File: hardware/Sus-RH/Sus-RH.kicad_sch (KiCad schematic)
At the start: 40 parts, among them J1 MX150_02x06_Vertical, J2 53307-2471, J4 Conn_01x06, J5 Conn_01x06, U1 TLV9002QDRQ1, U2 LDO40LPURY

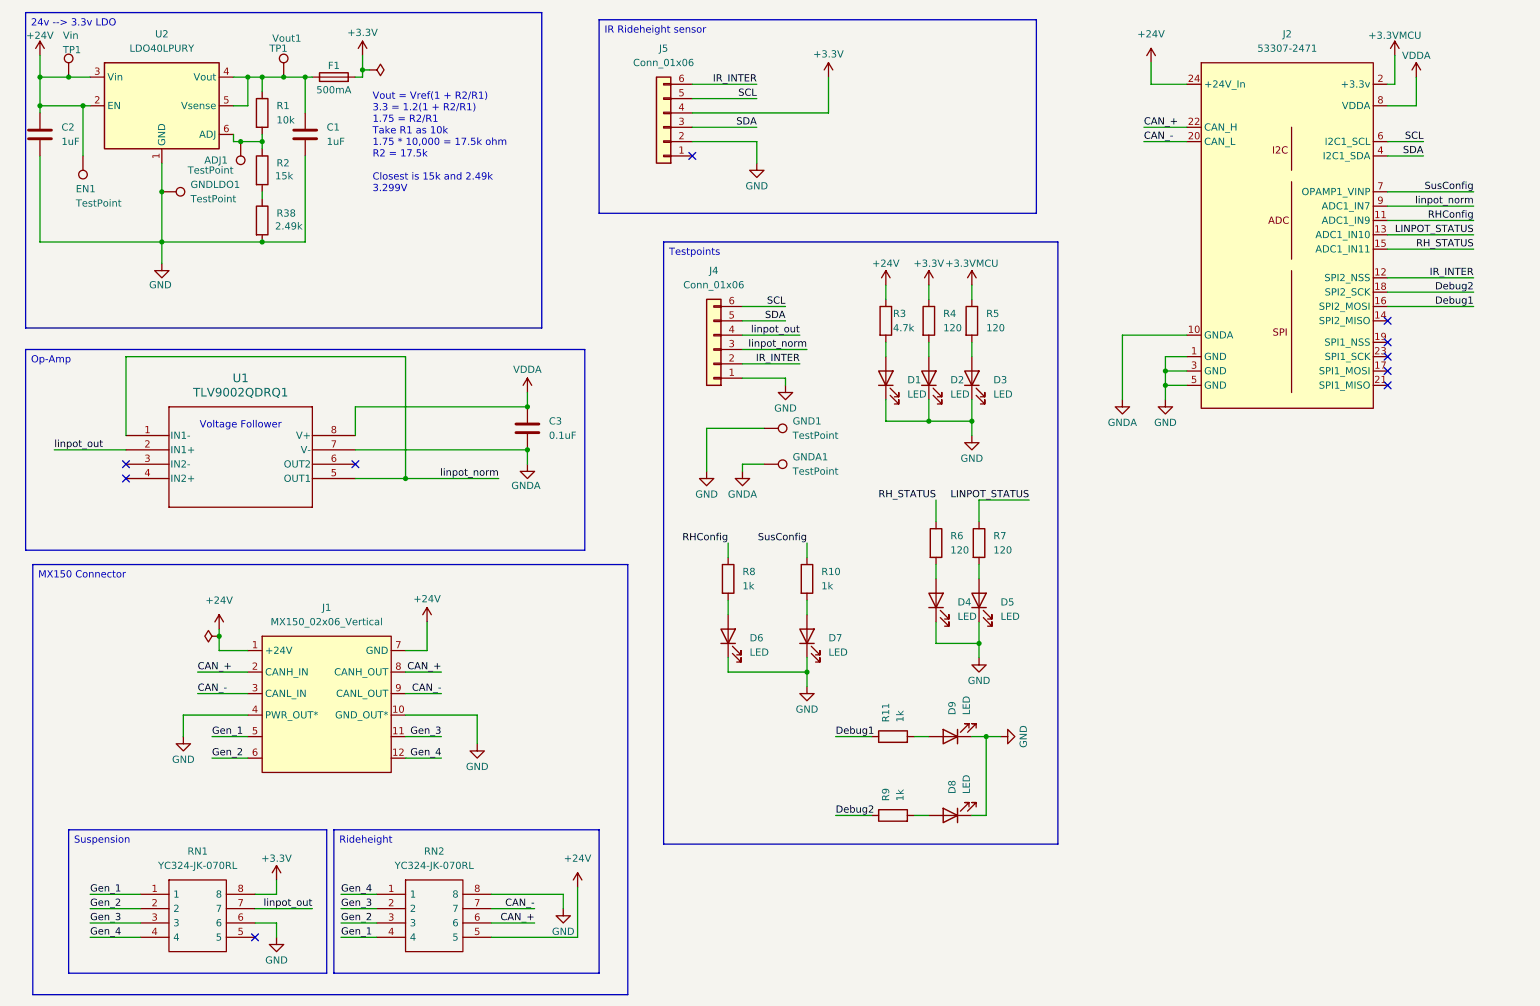
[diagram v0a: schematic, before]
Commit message: schematic changes: ldo switched out of qfn, op amp footprint fixed, resistor array changed. need add correct stm changes
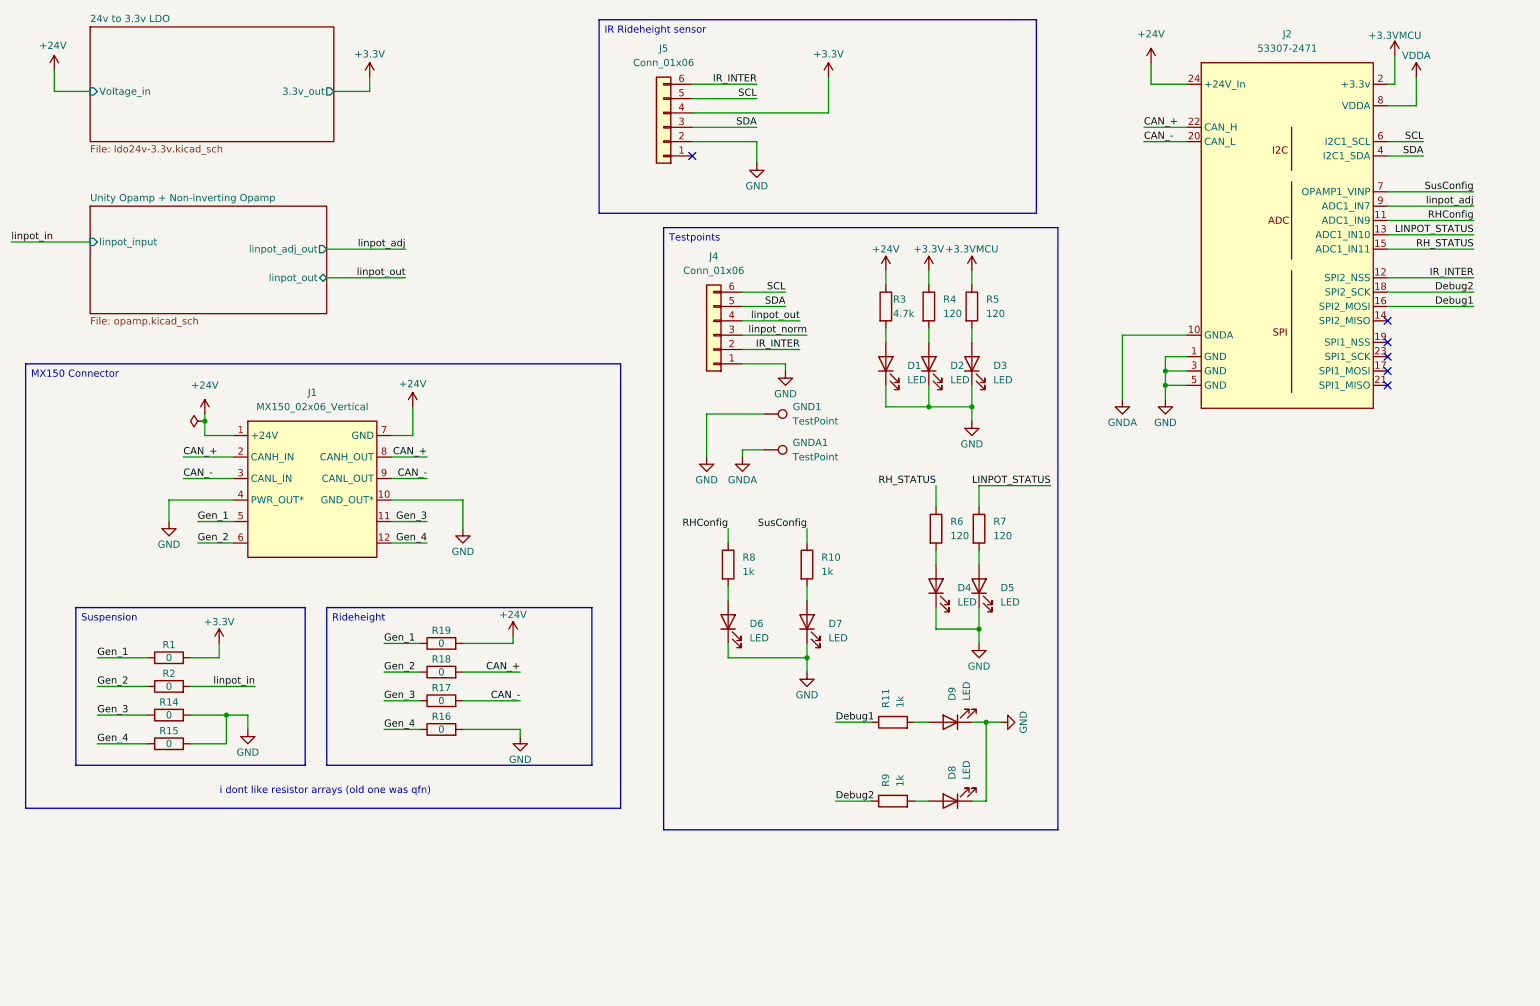
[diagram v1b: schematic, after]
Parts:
- removed ADJ1, EN1, GNDLDO1: TestPoint, TestPoint:TestPoint_Pad_D1.0mm, symbol Connector:TestPoint
- removed C1, C2: 1uF, Capacitor_SMD:C_0603_1608Metric_Pad1.08x0.95mm_HandSolder, symbol Device:C
- removed C3: 0.1uF, Capacitor_SMD:C_0603_1608Metric_Pad1.08x0.95mm_HandSolder, symbol Device:C
- removed F1: 500mA, Fuse:Fuseholder_Blade_Mini_Keystone_3568, symbol Device:Fuse
- removed R38: 2.49k, Resistor_SMD:R_0603_1608Metric_Pad0.98x0.95mm_HandSolder, symbol Device:R
- removed RN1, RN2: YC324-JK-070RL, 4pinRes:YC324JK07220RL, symbol YC324-JK-070RL:YC324-JK-070RL
- removed U1: TLV9002QDRQ1, footprints:SOIC8_D_TEX, symbol TLV9002QDRQ1:TLV9002QDRQ1
- removed U2: LDO40LPURY, Package_DFN_QFN:DFN-6-1EP_3x3mm_P0.95mm_EP1.7x2.6mm, symbol Regulator_Linear:LDO40LPURY
- removed Vin, Vout1: TP1, TestPoint:TestPoint_Pad_D1.0mm, symbol Connector:TestPoint
- added R14, R15, R16, R17, R18, R19: 0, symbol Device:R
- R1: value 10k -> 0; footprint Resistor_SMD:R_0603_1608Metric_Pad0.98x0.95mm_HandSolder -> (none); P/N CRCW060310K0FKEI -> (none)
- R2: value 15k -> 0; footprint Resistor_SMD:R_0603_1608Metric_Pad0.98x0.95mm_HandSolder -> (none); P/N CRCW060315K0FKEA -> (none)
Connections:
- net +24V: now also R19.2
- net +3.3V: now also R1.2
- net CAN_+: now also R18.2
- net CAN_-: now also R17.2
- net GND: now also R14.2, R15.2, R16.2
- net Gen_1: now also R1.1, R19.1
- net Gen_2: now also R2.1, R18.1
- net Gen_3: now also R14.1, R17.1
- net Gen_4: now also R15.1, R16.1
- net linpot_norm: no longer J2.9 (ADC1_IN7)
- net linpot_in: now reaches R2.2
- new net linpot_adj: J2.9 (ADC1_IN7)
- no-connect marks 10 -> 6
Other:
- added sheet 24v to 3.3v LDO (ldo24v-3.3v.kicad_sch)
- added sheet Unity Opamp + Non-inverting Opamp (opamp.kicad_sch)
- note added: "i dont like resistor arrays (old one was qfn)"
- note removed: "Voltage Follower"
- note removed: "Vout = Vref(1 + R2/R1) 3.3 = 1.2(1 + R2/R1) 1.75 = R2/R1 Take R1 as 10k 1.75 * 10,000 = 17.5k ohm R2 = 17.5k Closest is 15k and 2.49k 3.299V"
- moved on the sheet: D1, D2, D3, D4, D5, D6, D7, D8, D9, GND1, GNDA1, J1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

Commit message: finished sch + removed LDO
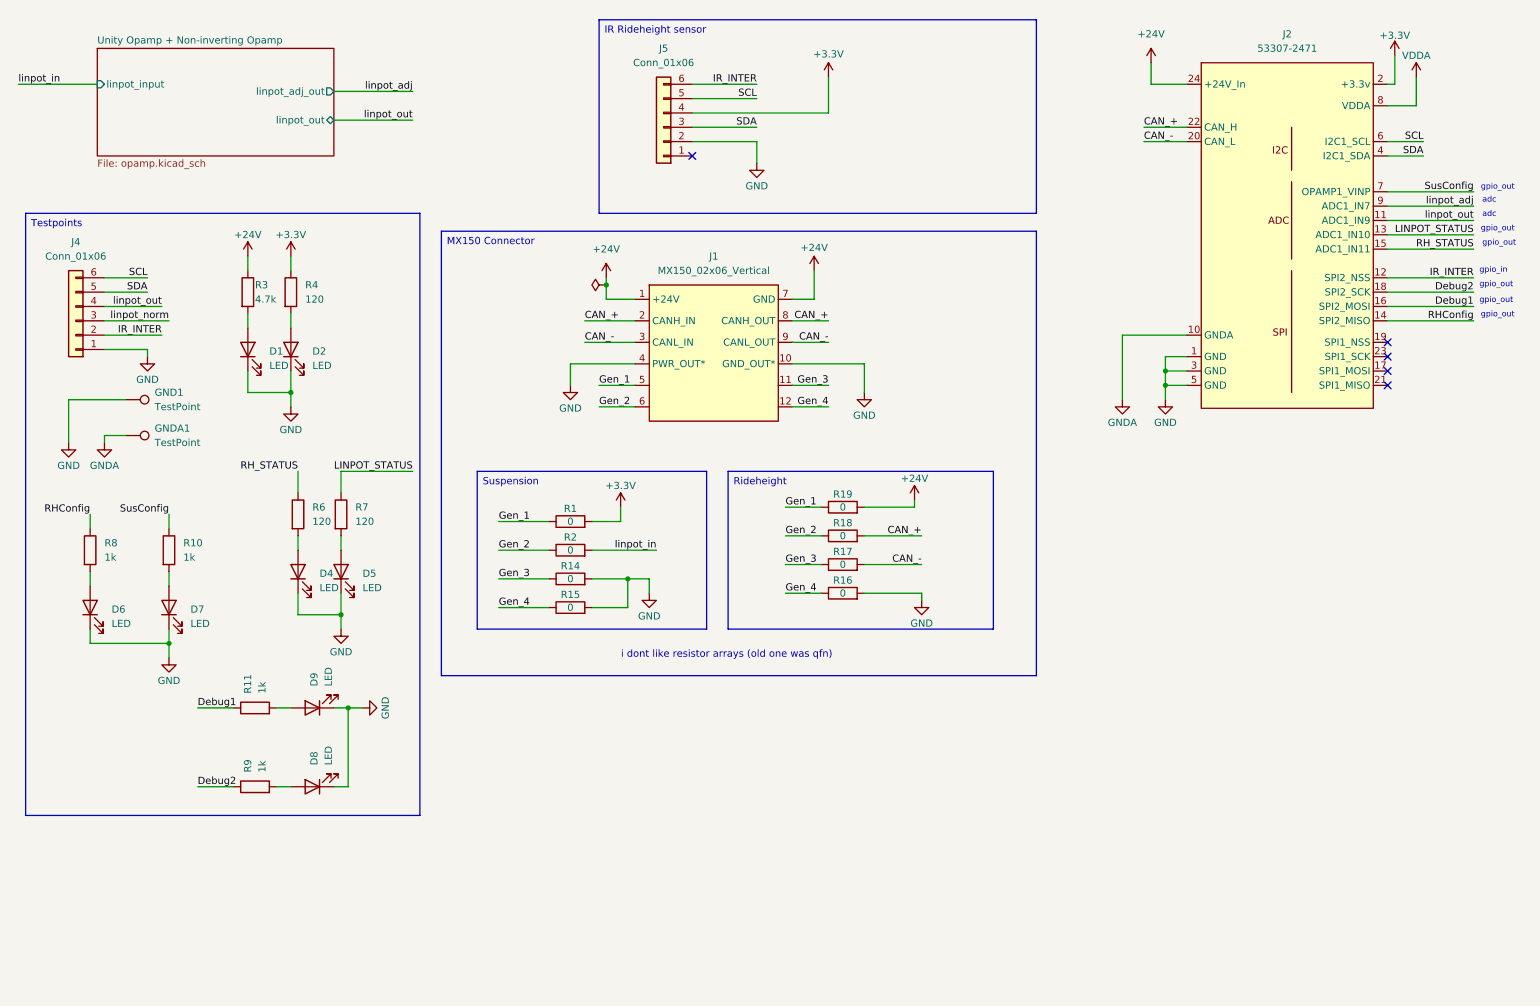
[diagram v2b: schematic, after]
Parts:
- removed D3: LED, LED_SMD:LED_0603_1608Metric_Pad1.05x0.95mm_HandSolder, symbol Device:LED
- removed R5: 120, Resistor_SMD:R_0603_1608Metric_Pad0.98x0.95mm_HandSolder, symbol Device:R
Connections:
- net +3.3VMCU is gone; now on net +3.3V: J2.2 (+3.3v)
- net RHConfig: now also J2.14 (SPI2_MISO); no longer J2.11 (ADC1_IN9)
- net linpot_out: now also J2.11 (ADC1_IN9)
- no-connect marks 6 -> 5
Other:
- removed sheet 24v to 3.3v LDO
- note added: "adc"
- note added: "gpio_in"
- note added: "gpio_out"
- moved on the sheet: D1, D2, D4, D5, D6, D7, D8, D9, GND1, GNDA1, J1, J4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

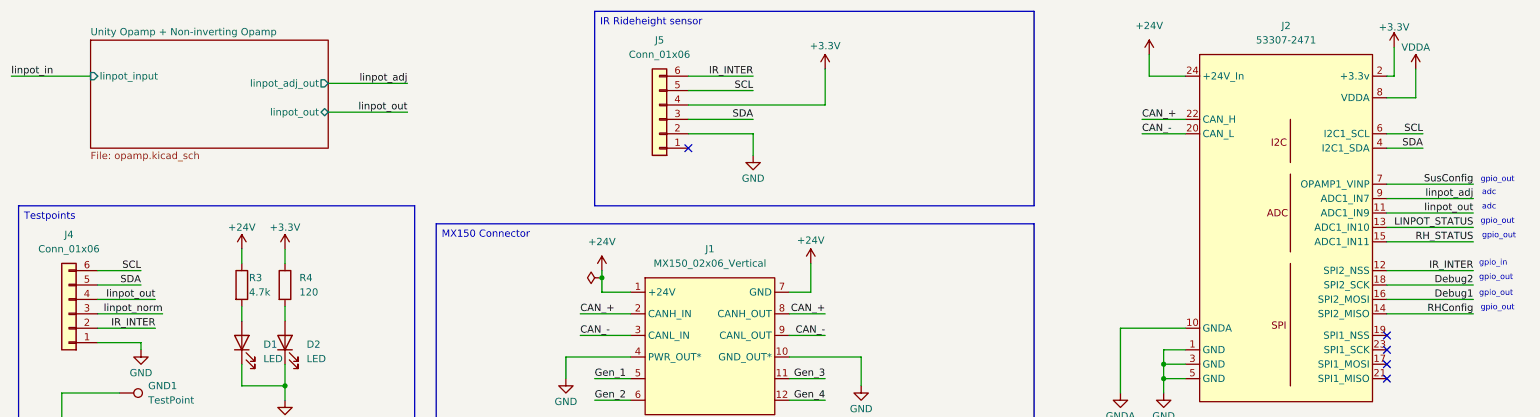
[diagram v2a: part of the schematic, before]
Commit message: removed LDO, added correct cube.
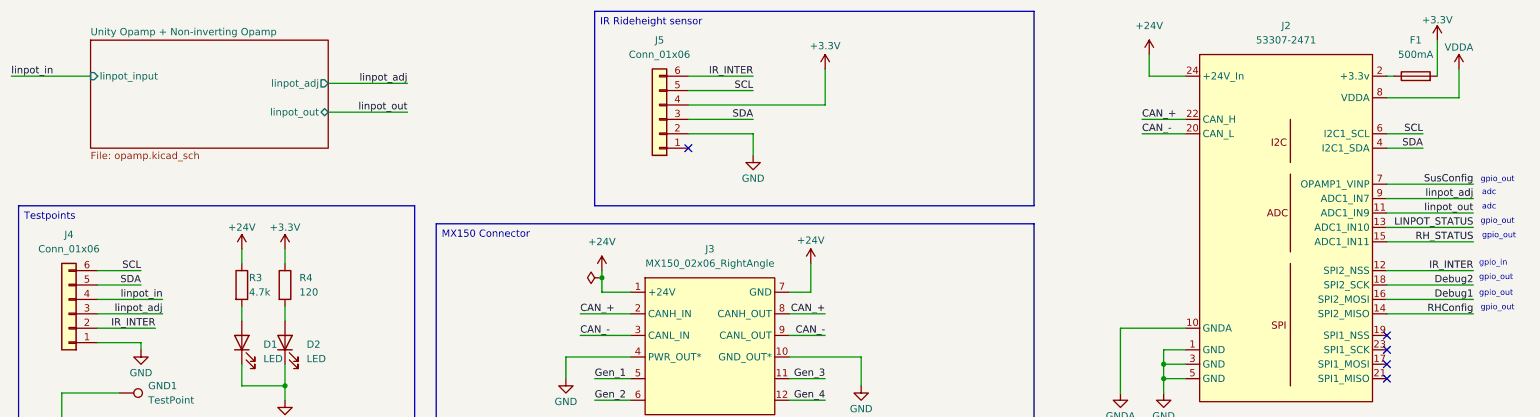
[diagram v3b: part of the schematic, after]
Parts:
- removed J1: MX150_02x06_Vertical, UTSVT_Connectors:MX150_02x06_Vertical, symbol utsvt_connectors:MX150_02x06_Vertical
- added F1: 500mA, Fuse:Fuseholder_Blade_Mini_Keystone_3568, symbol Device:Fuse
- added J3: MX150_02x06_RightAngle, UTSVT_Connectors:MX150_02x06_RightAngle, symbol utsvt_connectors:MX150_02x06_RightAngle
- R1, R14, R15, R16, R17, R18, R19, R2: footprint (none) -> Resistor_SMD:R_0603_1608Metric_Pad0.98x0.95mm_HandSolder
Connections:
- net linpot_norm is gone; now on net linpot_adj: J4.3 (Pin_3)
- net +24V: now also J3.1 (+24V), J3.7 (GND)
- net +3.3V: now also F1.2; no longer J2.2 (+3.3v)
- net CAN_+: now also J3.2 (CANH_IN), J3.8 (CANH_OUT)
- net CAN_-: now also J3.3 (CANL_IN), J3.9 (CANL_OUT)
- net GND: now also J3.10 (GND_OUT*), J3.4 (PWR_OUT*)
- net Gen_1: now also J3.5
- net Gen_2: now also J3.6
- net Gen_3: now also J3.11
- net Gen_4: now also J3.12
- net linpot_in: now also J4.4 (Pin_4)
- net linpot_out: no longer J4.4 (Pin_4)
- new net: F1.1, J2.2 (+3.3v)
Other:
- sheet Unity Opamp + Non-inverting Opamp ports: added linpot_adj; removed linpot_adj_out

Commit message: op-amp changes
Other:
- sheet Unity Opamp + Non-inverting Opamp renamed Unity Opamp + Adj Opamp
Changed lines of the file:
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@@
 			(color 0 0 0 0.0000)
 		)
-		(property "Sheetname" "Unity Opamp + Non-inverting Opamp"
+		(property "Sheetname" "Unity Opamp + Adj Opamp"
 			(at 29.21 22.1484 0)
 			(effects
